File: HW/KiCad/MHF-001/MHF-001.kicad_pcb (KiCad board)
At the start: 2 copper layers, 100 x 100 mm, 204 parts, among them J1 DE15_Socket_HighDensity_Mount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, J11 PPTC081LFBN-RC, J12 M20-9980345, J2 Mini-DIN-6, J3 Conn_Coaxial, J4 PJ-102AH, J5 USB_C_Receptacle_USB2.0_16P, J6 M20-9980345, J7 M20-9980245, M3 CY7C109D-10ZXI, M5 CY7C109D-10ZXI, Q1 BC107, Q2 PMV48XP, U1 NCP1117-5.0_SOT223, U10 74HC245, U11 74HC245, U12 74HC245, U13 LMV358IDGKR, U14 LP2985-3.3, U15 ATMEGA16U2-MU, U2 74HC14, U3 74LS08, U4 74HC165, U5 ATmega2560-16A, U6 74AHC373PW, U7 74HC595, U8 74HC595, U9 74HC157, Y1 CSTNE16M0V530000R0, Y2 LFXTAL003240BULK

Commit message: +3d models, +Pins.rst, some reorganisation
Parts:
- removed C17: 22p, Capacitor_SMD:C_0603_1608Metric
- removed C18, C19: 100n, Capacitor_SMD:C_0603_1608Metric
- removed D4: CGRB307-G, Diode_SMD:D_SMB
- removed D5, D8: YELLOW, LED_SMD:LED_0805_2012Metric
- removed D6: GREEN, LED_SMD:LED_0805_2012Metric
- removed D7: CD1206-S01575, Diode_SMD:D_1206_3216Metric
- removed FB1, FB2: 1kΩ@100MHz, Inductor_SMD:L_0805_2012Metric
- removed FID1, FID2, FID3, FID4: Fiducial, Fiducial:Fiducial_1mm_Mask3mm
- removed J11: PPTC081LFBN-RC, Connector_PinSocket_2.54mm:PinSocket_1x08_P2.54mm_Vertical
- removed J12, J6: M20-9980345, Connector_PinHeader_2.54mm:PinHeader_2x03_P2.54mm_Vertical
- removed J4: PJ-102AH, Connector_BarrelJack:BarrelJack_Kycon_KLDX-0202-xC_Horizontal
- removed J7: M20-9980245, Arduino Mega 2560:CONN_M20-9980245_HRW
- removed Q2: PMV48XP, Package_TO_SOT_SMD:SC-59
- removed RN1, RN5: 10k, Resistor_SMD:R_Array_Convex_4x0612
- removed RN2: 22R, Resistor_SMD:R_Array_Convex_4x0612
- removed RN3, RN4: 1k, Resistor_SMD:R_Array_Convex_4x0612
- removed RV1, RV2: 5pF@1MHz, Resistor_SMD:R_0603_1608Metric
- removed U5: ATmega2560-16A, Package_QFP:TQFP-100_14x14mm_P0.5mm
- added H1: MountingHole, MountingHole:MountingHole_3.2mm_M3, F.Cu at (31.6, 29.6)
- added H2: MountingHole, MountingHole:MountingHole_3.2mm_M3, F.Cu at (118.9, 30.5)
- added H3: MountingHole, MountingHole:MountingHole_3.2mm_M3, F.Cu at (122.8, 106.6)
- added H4: MountingHole, MountingHole:MountingHole_3.2mm_M3, F.Cu at (38.7, 107.7)
- added J8: AVR-ISP-6, Connector_PinHeader_2.54mm:PinHeader_2x03_P2.54mm_Vertical, F.Cu at (160.4, 118.9)
- added LED1: LED, LED_SMD:LED_0201_0603Metric, F.Cu at (166.7, 117.5)
- added LED2: LED, LED_SMD:LED_0201_0603Metric, F.Cu at (166.7, 119.2)
- added LED3: LED, LED_SMD:LED_0201_0603Metric, F.Cu at (166.7, 121.0)
- added LED4: LED, LED_SMD:LED_0201_0603Metric, F.Cu at (166.7, 122.7)
- added R28: 1k, Resistor_SMD:R_0603_1608Metric, F.Cu at (151.0, 90.3)
- added R29: 1M, Resistor_SMD:R_0603_1608Metric, F.Cu at (151.0, 92.8)
- added R30: 22, Resistor_SMD:R_0603_1608Metric, F.Cu at (151.0, 95.3)
- added R31: 22, Resistor_SMD:R_0603_1608Metric, F.Cu at (151.0, 97.8)
- added R32: ---, Resistor_SMD:R_0603_1608Metric, F.Cu at (151.0, 100.3)
- added R33: ---, Resistor_SMD:R_0603_1608Metric, F.Cu at (151.0, 102.9)
- added R34: 6k8, Resistor_SMD:R_0603_1608Metric, F.Cu at (155.0, 85.3)
- added R35: 6k8, Resistor_SMD:R_0603_1608Metric, F.Cu at (155.0, 87.8)
- added R36: 1k, Resistor_SMD:R_0603_1608Metric, F.Cu at (155.0, 90.3)
- added R37: 10k, Resistor_SMD:R_0603_1608Metric, F.Cu at (155.0, 92.8)
- C11: value 100n -> 10M; footprint Capacitor_SMD:C_0603_1608Metric -> Capacitor_SMD:C_1206_3216Metric
- C12, C15: value 1u -> 100n
- C16: value 22p -> 100n
- C2, C7: value 47u -> 100n; footprint Arduino Mega 2560:CAP_EEHZA1E470P -> Capacitor_SMD:C_0603_1608Metric
- D2: value YELLOW -> D; footprint LED_SMD:LED_0805_2012Metric -> Diode_SMD:D_1206_3216Metric
- D3: value CD1206-S01575 -> D; footprint Diode_SMD:D_1206_3216Metric -> Diode_SMD:D_1210_3225Metric
- F1: value MF-MSMF050-2 -> Polyfuse; footprint Fuse:Fuse_1812_4532Metric_Pad1.30x3.40mm_HandSolder -> Fuse:Fuse_1206_3216Metric_Pad1.42x1.75mm_HandSolder
- J5: value USB_C_Receptacle_USB2.0_16P -> USB_B_Micro; footprint Connector_USB:USB_C_Receptacle_GCT_USB4105-xx-A_16P_TopMnt_Horizontal -> Connector_USB:USB_Micro-B_XKB_U254-051T-4BH83-F1S
- JP89, JP90: value SolderJumper_2_Open -> SolderJumper_2_Bridged; footprint Jumper:SolderJumper-2_P1.3mm_Open_Pad1.0x1.5mm -> Jumper:SolderJumper-2_P1.3mm_Bridged_Pad1.0x1.5mm
- R24: value 1M -> 22
- R25: value 5k1 -> 22
- R26: value 5k1 -> 10k
- U1: value NCP1117-5.0_SOT223 -> ATMEGA2560-16AU; footprint Package_TO_SOT_SMD:SOT-223-3_TabPin2 -> Package_QFP:TQFP-100_14x14mm_P0.5mm
- U13: value LMV358IDGKR -> CH340G; footprint Package_SO:MSOP-8_3x3mm_P0.65mm -> Package_SO:SOIC-16_3.9x9.9mm_P1.27mm
- U14: value LP2985-3.3 -> AMS1117-5.0; footprint Package_TO_SOT_SMD:SOT-23-5 -> Package_TO_SOT_SMD:SOT-223-3_TabPin2
- U15: value ATMEGA16U2-MU -> AMS1117-3.3; footprint Package_DFN_QFN:VQFN-32-1EP_5x5mm_P0.5mm_EP3.1x3.1mm -> Package_TO_SOT_SMD:SOT-223-3_TabPin2
- Y1: value CSTNE16M0V530000R0 -> 16 MHz; footprint Crystal:Resonator_SMD_Murata_CSTxExxV-3Pin_3.0x1.1mm -> Crystal:Crystal_SMD_HC49-SD
- Y2: value LFXTAL003240BULK -> 12 MHz; footprint Crystal:Crystal_HC49-4H_Vertical -> Crystal:Crystal_SMD_HC49-SD
- moved U1 185.2 mm to (65.3, 94.9)
- moved JP89 163.0 mm to (1.68, 1.27)
- moved JP90 163.0 mm to (1.68, 4.83)
- moved J5 161.1 mm to (30.0, 99.5), turned to -90 degrees
- moved S1 132.6 mm to (156.6, 130.4)
- moved F1 115.7 mm to (171.0, 135.7)
- moved U15 100.7 mm to (145.9, 116.6)
- moved C16 94.7 mm to (147.0, 97.8)
- moved U7 93.9 mm to (-12.2, 96.2), turned to 0 degrees
- moved D3 92.7 mm to (170.8, 118.8)
- moved R24 92.3 mm to (147.0, 100.3)
- moved R26 92.2 mm to (151.0, 85.3)
- moved R25 91.7 mm to (147.0, 102.9)
- moved R27 91.7 mm to (151.0, 87.8)
- moved C5 91.5 mm to (143.0, 92.8)
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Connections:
- net Net-(JP16-B) renamed VGA Latch
- net Net-(JP41-B) renamed VGA data 0
- net Net-(JP42-B) renamed VGA data 1
- net Net-(JP43-B) renamed VGA data 2
- net Net-(JP44-B) renamed VGA data 3
- net Net-(JP45-B) renamed VGA data 4
- net Net-(JP46-B) renamed VGA data 5
- net Net-(JP47-B) renamed VGA data 6
- net Net-(JP48-B) renamed VGA data 7
- C10 pad 1: USBVCC -> +5V
- C11 pad 1: +5V -> Net-(D3-K)
- C12 pad 1: Net-(U15-UCAP) -> Reset
- C13 pad 2: +5V -> XTAL1
- C14 pad 2: CMP -> XTAL2
- C15 pad 1: GND -> +5V
- C15 pad 2: +3.3V -> GND
- C16 pad 1: Net-(U15-XTAL1) -> +3.3V
- C2 pad 1: VCC -> GND
- C2 pad 2: GND -> Net-(U13-V3)
- C3 pad 1: RESET -> GND
- C3 pad 2: GND -> Net-(U13-XO)
- C4 pad 1: VCC -> GND
- C4 pad 2: GND -> Net-(U13-XI)
- C9 pad 1: +5V -> Reset
- C9 pad 2: GND -> Net-(U13-~{DTR})
- D2 pad 1: TXL -> +5V
- D2 pad 2: Net-(D2-A) -> Reset
- D3 pad 1: +5V -> Net-(D3-K)
- D3 pad 2: RESET2 -> VIN
- F1 pad 1: USBVCC -> +5V
- F1 pad 2: XVCC -> Net-(J5-VBUS)
- JP10 pad 2: unconnected-(JP10-B-Pad2) -> SCK
- JP11 pad 2: unconnected-(JP11-B-Pad2) -> MOSI
- JP12 pad 2: unconnected-(JP12-B-Pad2) -> MISO
- JP25 pad 2: unconnected-(JP25-B-Pad2) -> SCL
- JP26 pad 2: unconnected-(JP26-B-Pad2) -> SDA
- JP33 pad 2: unconnected-(JP33-B-Pad2) -> TX
- JP34 pad 2: unconnected-(JP34-B-Pad2) -> RX
- JP35 pad 2: unconnected-(JP35-B-Pad2) -> CTS
- JP36 pad 2: Inside -> RTS
- JP39 pad 2: unconnected-(JP39-B-Pad2) -> Inside
- JP49 pad 2: unconnected-(JP49-B-Pad2) -> WE
- JP50 pad 2: unconnected-(JP50-B-Pad2) -> RD
- JP51 pad 2: unconnected-(JP51-B-Pad2) -> ALE
- JP52 pad 2: unconnected-(JP52-B-Pad2) -> XAA16
- JP57 pad 2: unconnected-(JP57-B-Pad2) -> Ib
- JP58 pad 2: unconnected-(JP58-B-Pad2) -> Bb
- JP59 pad 2: unconnected-(JP59-B-Pad2) -> Gb
- JP60 pad 2: unconnected-(JP60-B-Pad2) -> Rb
- JP61 pad 2: unconnected-(JP61-B-Pad2) -> If
- JP62 pad 2: unconnected-(JP62-B-Pad2) -> Bf
- JP63 pad 2: unconnected-(JP63-B-Pad2) -> Gf
- JP64 pad 2: unconnected-(JP64-B-Pad2) -> Rf
- JP89 pad 1: GND -> PS2 Clock
- JP89 pad 2: GND -> Net-(D1-K)
- JP9 pad 2: unconnected-(JP9-B-Pad2) -> SS
- JP90 pad 1: RESET -> PS2 Data
- JP90 pad 2: RESET -> /Data
- M3 pad 10: PG3 -> XAA16
- M3 pad 32: PG0 -> RD
- M3 pad 5: PG1 -> WE
- M5 pad 10: unconnected-(M5-A16-Pad10) -> XAA16
- M5 pad 7: unconnected-(M5-A15-Pad7) -> Shared_Address_A15
- R16 pad 2: Mega_6309_data0 -> Ib
- R17 pad 2: Mega_6309_data1 -> Bb
- R18 pad 2: Mega_6309_data2 -> Gb
- R19 pad 2: Mega_6309_data3 -> Rb
- R20 pad 2: Mega_6309_data4 -> If
- R21 pad 2: Mega_6309_data5 -> Bf
- R22 pad 2: Mega_6309_data6 -> Gf
- R23 pad 2: Mega_6309_data7 -> Rf
- R24 pad 1: XTAL1 -> RD+
- R24 pad 2: XTAL2 -> Net-(J5-D+)
- R25 pad 1: GND -> RD-
- R25 pad 2: CC1 -> Net-(J5-D-)
- R26 pad 1: GND -> +5V
- R26 pad 2: CC2 -> Reset
- R27 pad 1: Net-(U15-XTAL1) -> Net-(U13-XI)
- R27 pad 2: Net-(U15-PC0) -> Net-(U13-XO)
- R5 pad 1: SIGNAL_RCA -> Bb
- S1 pad 3: RESET -> Reset
- S1 pad 4: RESET -> Reset
- S1 pad 5: unconnected-(S1-Pad5) -> GND
- U1 pad 1: GND -> PG5
- U1 pad 2: +5V -> PE0
- U1 pad 3: VCC -> PE1
- U13 pad 1: L13 -> GND
- U13 pad 2: L13 -> M8TXD
- U13 pad 3: PB7 -> M8RXD
- U13 pad 4: GND -> Net-(U13-V3)
- U13 pad 5: CMP -> RD+
- U13 pad 6: +3.3V -> RD-
- U13 pad 7: GATE_CMD -> Net-(U13-XI)
- U13 pad 8: +5V -> Net-(U13-XO)
- U14 pad 1: +5V -> GND
- U14 pad 2: GND -> +5V
- U14 pad 3: +5V -> Net-(D3-K)
- U15 pad 1: Net-(U15-XTAL1) -> GND
- U15 pad 2: Net-(U15-PC0) -> +3.3V
- U15 pad 3: GND -> +5V
- U3 pad 1: SIGNAL_RCA -> Bb
- U6 pad 11: PG2 -> ALE
- U9 pad 10: unconnected-(U9-I1c-Pad10) -> Gf
- U9 pad 11: unconnected-(U9-I0c-Pad11) -> Gb
- U9 pad 13: unconnected-(U9-I1d-Pad13) -> Bf
- U9 pad 14: unconnected-(U9-I0d-Pad14) -> Bb
- U9 pad 2: unconnected-(U9-I0a-Pad2) -> Ib
- U9 pad 3: unconnected-(U9-I1a-Pad3) -> If
- U9 pad 5: unconnected-(U9-I0b-Pad5) -> Rb
- U9 pad 6: unconnected-(U9-I1b-Pad6) -> Rf
- Y1 pad 2: GND -> XTAL1
- Y2 pad 1: Net-(U15-PC0) -> Net-(U13-XO)
- Y2 pad 2: Net-(U15-XTAL1) -> Net-(U13-XI)

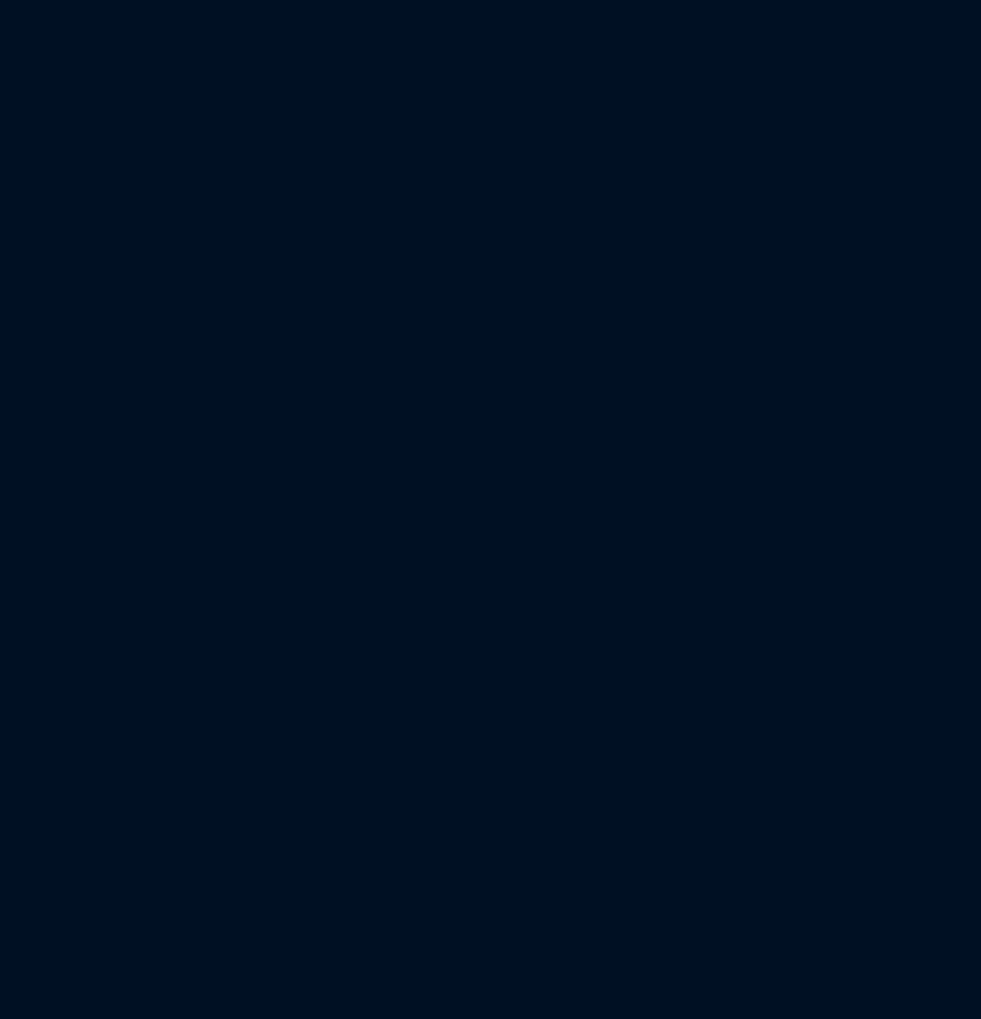
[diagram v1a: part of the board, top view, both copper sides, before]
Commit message: +Comp24 footprint
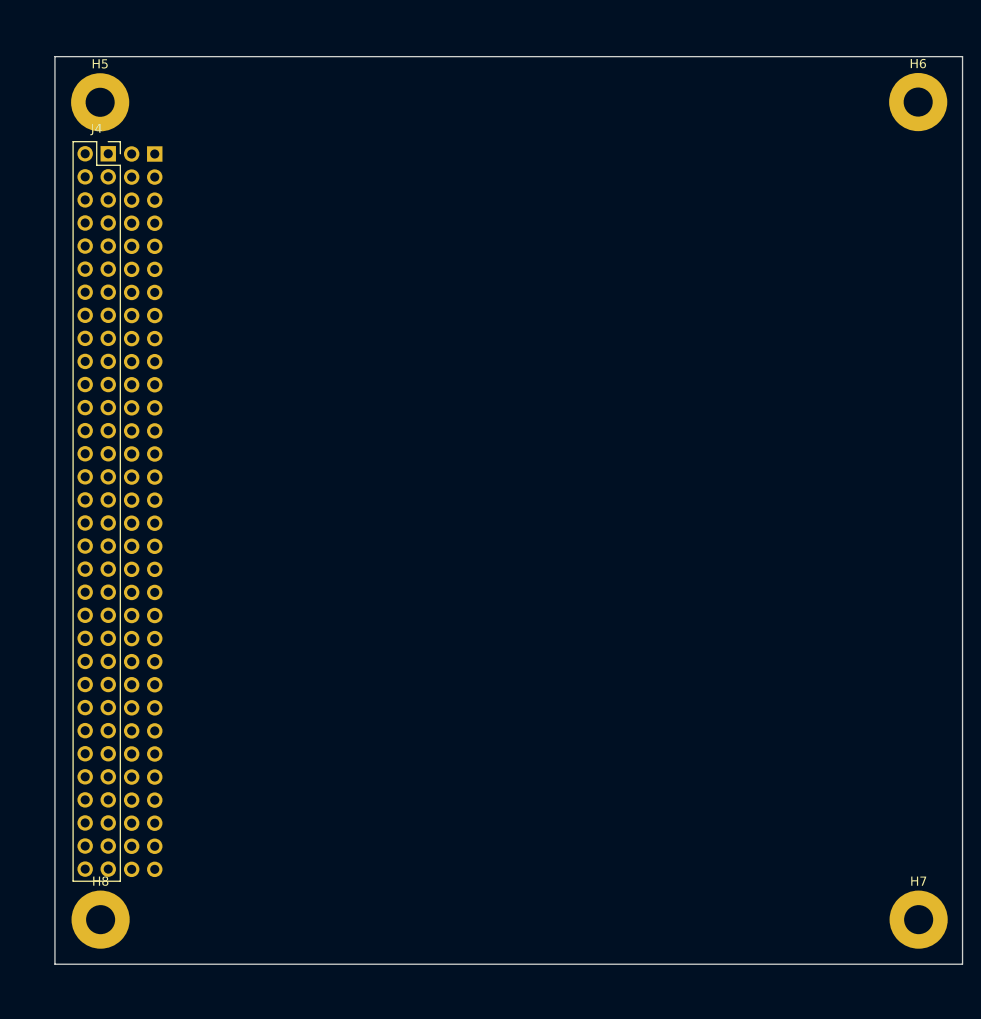
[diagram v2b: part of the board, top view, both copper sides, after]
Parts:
- added H5: MountingHole, MountingHole:MountingHole_3.2mm_M3_Pad, F.Cu at (186.1, 24.5)
- added H6: MountingHole, MountingHole:MountingHole_3.2mm_M3_Pad, F.Cu at (276.2, 24.5)
- added H7: MountingHole, MountingHole:MountingHole_3.2mm_M3_Pad, F.Cu at (276.2, 114.5)
- added H8: MountingHole, MountingHole:MountingHole_3.2mm_M3_Pad, F.Cu at (186.2, 114.5)
- added J4: Conn_02x32_Odd_Even, Connector_PinSocket_2.54mm:PinSocket_2x32_P2.54mm_Vertical, F.Cu at (187.0, 30.2)
- added J6: Conn_02x32_Odd_Even, Connector_PinHeader_2.54mm:PinHeader_2x32_P2.54mm_Vertical, B.Cu at (192.1, 30.2)
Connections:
- net /Data renamed Data
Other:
- board size 100 x 100 mm -> 252.9 x 100.2 mm

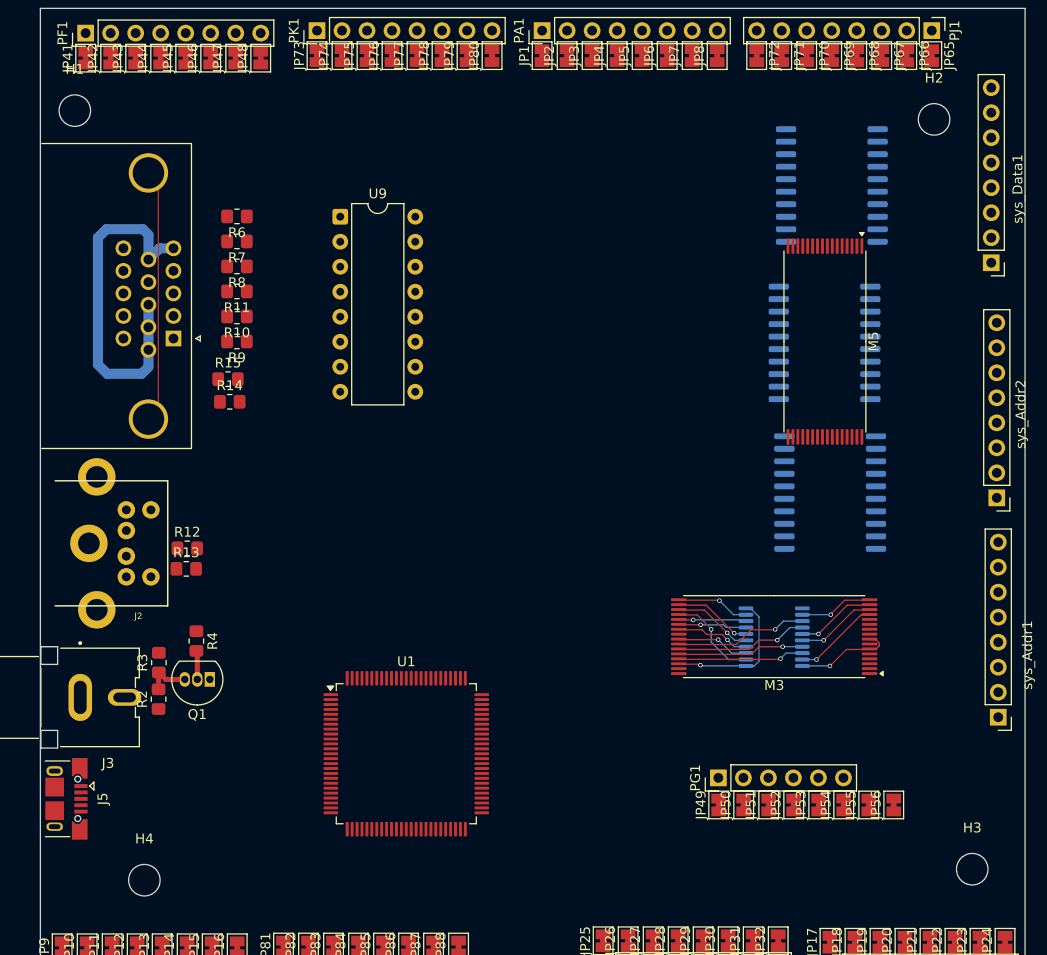
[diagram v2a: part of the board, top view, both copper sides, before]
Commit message: - mounting holes
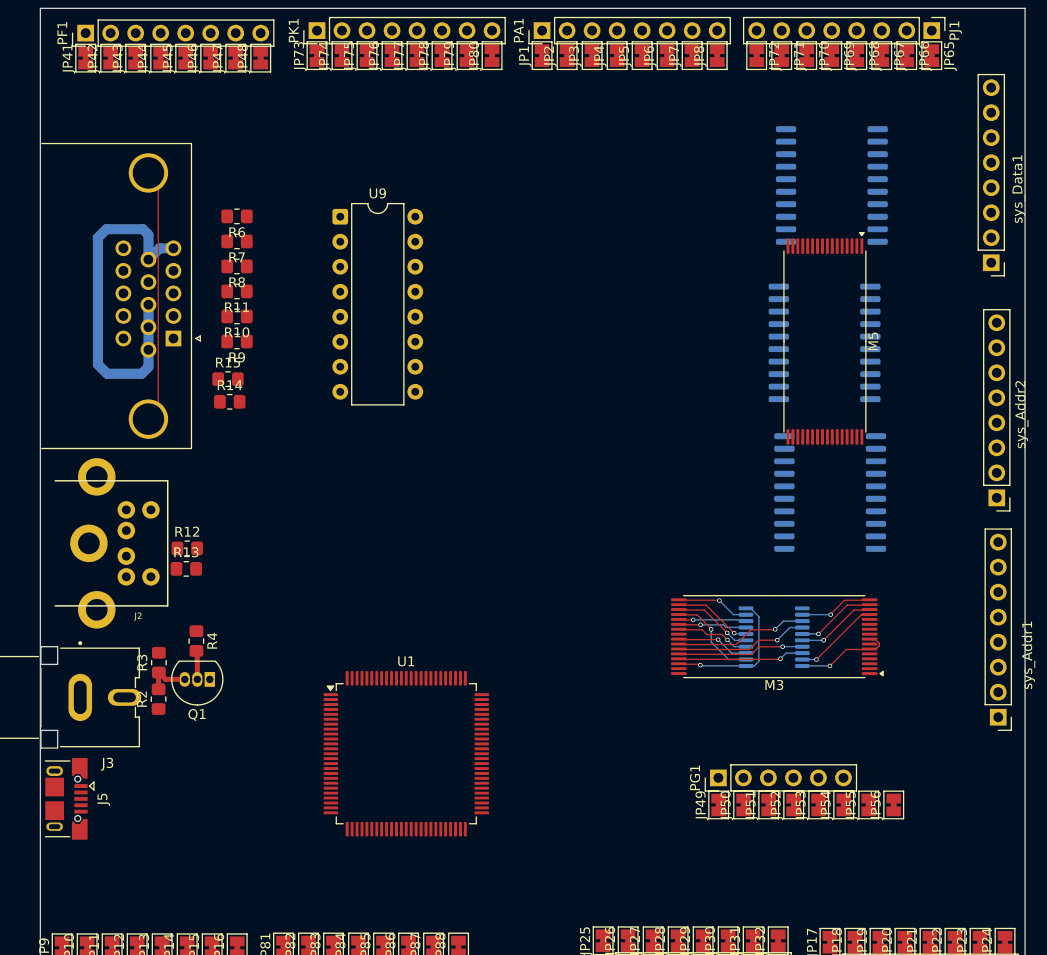
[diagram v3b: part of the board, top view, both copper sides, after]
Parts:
- removed H1, H2, H3, H4: MountingHole, MountingHole:MountingHole_3.2mm_M3

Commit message: schema MHF-001 maybe OK
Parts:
- removed sys_Addr1, sys_Addr2, sys_Data1: Conn_01x08, Connector_PinHeader_2.54mm:PinHeader_1x08_P2.54mm_Vertical
- added J10: I2C, Connector_PinHeader_2.54mm:PinHeader_1x04_P2.54mm_Vertical, F.Cu at (139.7, 142.2)
- added J11: POWER, Connector_PinHeader_2.54mm:PinHeader_2x03_P2.54mm_Vertical, F.Cu at (132.1, 160.0)
- added J7: SPI, Connector_PinHeader_2.54mm:PinHeader_1x06_P2.54mm_Vertical, F.Cu at (132.1, 142.2)
- added J9: Serial, Connector_PinHeader_2.54mm:PinHeader_1x06_P2.54mm_Vertical, F.Cu at (134.6, 142.2)
- added JP100: SolderJumper_3_Open, Jumper:SolderJumper-3_P1.3mm_Open_RoundedPad1.0x1.5mm, F.Cu at (127.0, 152.4)
- added JP101: SolderJumper_3_Open, Jumper:SolderJumper-3_P1.3mm_Open_RoundedPad1.0x1.5mm, F.Cu at (127.0, 157.5)
- added JP102: SolderJumper_3_Open, Jumper:SolderJumper-3_P1.3mm_Open_RoundedPad1.0x1.5mm, F.Cu at (95.5, 141.5)
- added JP103: SolderJumper_3_Open, Jumper:SolderJumper-3_P1.3mm_Open_RoundedPad1.0x1.5mm, F.Cu at (95.5, 146.6)
- added JP104: SolderJumper_3_Open, Jumper:SolderJumper-3_P1.3mm_Open_RoundedPad1.0x1.5mm, F.Cu at (95.5, 149.1)
- added JP105: SolderJumper_3_Open, Jumper:SolderJumper-3_P1.3mm_Open_RoundedPad1.0x1.5mm, F.Cu at (95.5, 154.2)
- added JP106: SolderJumper_3_Open, Jumper:SolderJumper-3_P1.3mm_Open_RoundedPad1.0x1.5mm, F.Cu at (95.5, 156.7)
- added JP107: SolderJumper_3_Open, Jumper:SolderJumper-3_P1.3mm_Open_RoundedPad1.0x1.5mm, F.Cu at (95.5, 161.8)
- added JP108: SolderJumper_3_Open, Jumper:SolderJumper-3_P1.3mm_Open_RoundedPad1.0x1.5mm, F.Cu at (95.5, 164.4)
- added JP92: SolderJumper_3_Open, Jumper:SolderJumper-3_P1.3mm_Open_RoundedPad1.0x1.5mm, F.Cu at (119.4, 142.2)
- added JP93: SolderJumper_3_Open, Jumper:SolderJumper-3_P1.3mm_Open_RoundedPad1.0x1.5mm, F.Cu at (119.4, 144.8)
- added JP94: SolderJumper_3_Open, Jumper:SolderJumper-3_P1.3mm_Open_RoundedPad1.0x1.5mm, F.Cu at (119.4, 149.9)
- added JP95: SolderJumper_3_Open, Jumper:SolderJumper-3_P1.3mm_Open_RoundedPad1.0x1.5mm, F.Cu at (119.4, 152.4)
- added JP96: SolderJumper_3_Open, Jumper:SolderJumper-3_P1.3mm_Open_RoundedPad1.0x1.5mm, F.Cu at (119.4, 157.5)
- added JP97: SolderJumper_3_Open, Jumper:SolderJumper-3_P1.3mm_Open_RoundedPad1.0x1.5mm, F.Cu at (127.0, 142.2)
- added JP98: SolderJumper_3_Open, Jumper:SolderJumper-3_P1.3mm_Open_RoundedPad1.0x1.5mm, F.Cu at (127.0, 144.8)
- added JP99: SolderJumper_3_Open, Jumper:SolderJumper-3_P1.3mm_Open_RoundedPad1.0x1.5mm, F.Cu at (127.0, 149.9)
- added LED5: LED, LED_SMD:LED_0805_2012Metric, F.Cu at (100.5, 146.6)
- added LED6: LED, LED_SMD:LED_0805_2012Metric, F.Cu at (105.0, 146.7)
- added R38: 1k, Resistor_SMD:R_0805_2012Metric_Pad1.20x1.40mm_HandSolder, F.Cu at (100.5, 141.5)
- added R39: 1k, Resistor_SMD:R_0805_2012Metric_Pad1.20x1.40mm_HandSolder, F.Cu at (100.5, 144.0)
- C10, C12, C13, C14, C15, C16, C2, C3, C4, C5, C6, C7, C8, C9: footprint Capacitor_SMD:C_0603_1608Metric -> Capacitor_SMD:C_0603_1608Metric_Pad1.08x0.95mm_HandSolder
- C11: footprint Capacitor_SMD:C_1206_3216Metric -> Capacitor_SMD:C_0603_1608Metric_Pad1.08x0.95mm_HandSolder
- J6: value Conn_02x32_Odd_Even -> 02x32
- LED1, LED2, LED3, LED4: footprint LED_SMD:LED_0201_0603Metric -> LED_SMD:LED_0805_2012Metric
- R24, R25, R26, R27, R28, R29, R30, R31, R32, R33, R34, R35, R36, R37: footprint Resistor_SMD:R_0603_1608Metric -> Resistor_SMD:R_0603_1608Metric_Pad0.98x0.95mm_HandSolder
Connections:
- net Data renamed /Data
- net Net-(U11-A->B) renamed G_A_DIR
- J4 pad 1: D0 -> +5V
- J4 pad 10: unconnected-(J4-Pin_10-Pad10) -> D7
- J4 pad 11: unconnected-(J4-Pin_11-Pad11) -> A0
- J4 pad 12: unconnected-(J4-Pin_12-Pad12) -> A1
- J4 pad 13: unconnected-(J4-Pin_13-Pad13) -> A2
- J4 pad 14: unconnected-(J4-Pin_14-Pad14) -> A3
- J4 pad 15: unconnected-(J4-Pin_15-Pad15) -> A4
- J4 pad 16: unconnected-(J4-Pin_16-Pad16) -> A5
- J4 pad 17: unconnected-(J4-Pin_17-Pad17) -> A6
- J4 pad 18: unconnected-(J4-Pin_18-Pad18) -> A7
- J4 pad 19: unconnected-(J4-Pin_19-Pad19) -> A8
- J4 pad 2: D1 -> +5V
- J4 pad 20: unconnected-(J4-Pin_20-Pad20) -> A9
- J4 pad 21: unconnected-(J4-Pin_21-Pad21) -> A10
- J4 pad 22: unconnected-(J4-Pin_22-Pad22) -> A11
- J4 pad 23: unconnected-(J4-Pin_23-Pad23) -> A12
- J4 pad 24: unconnected-(J4-Pin_24-Pad24) -> A13
- J4 pad 25: unconnected-(J4-Pin_25-Pad25) -> A14
- J4 pad 26: unconnected-(J4-Pin_26-Pad26) -> A15
- J4 pad 27: unconnected-(J4-Pin_27-Pad27) -> A16
- J4 pad 28: unconnected-(J4-Pin_28-Pad28) -> B16
- J4 pad 29: unconnected-(J4-Pin_29-Pad29) -> A_BUS
- J4 pad 3: D2 -> D0
- J4 pad 30: unconnected-(J4-Pin_30-Pad30) -> B_BUS
- J4 pad 31: unconnected-(J4-Pin_31-Pad31) -> A_HALT
- J4 pad 32: unconnected-(J4-Pin_32-Pad32) -> B_HALT
- J4 pad 33: unconnected-(J4-Pin_33-Pad33) -> A_READ
- J4 pad 34: unconnected-(J4-Pin_34-Pad34) -> B_READ
- J4 pad 35: unconnected-(J4-Pin_35-Pad35) -> A_WRITE
- J4 pad 36: unconnected-(J4-Pin_36-Pad36) -> B_WRITE
- J4 pad 37: unconnected-(J4-Pin_37-Pad37) -> A_SHARE_BUSY
- J4 pad 38: unconnected-(J4-Pin_38-Pad38) -> B_SHARE_BUSY
- J4 pad 39: unconnected-(J4-Pin_39-Pad39) -> A_SHARE_DIRTY
- J4 pad 4: D3 -> D1
- J4 pad 40: unconnected-(J4-Pin_40-Pad40) -> B_SHARE_DIRTY
- J4 pad 41: unconnected-(J4-Pin_41-Pad41) -> A_SHARE_GRANTED
- J4 pad 42: unconnected-(J4-Pin_42-Pad42) -> B_SHARE_GRANTED
- J4 pad 43: unconnected-(J4-Pin_43-Pad43) -> A_SHARE_REQUEST
- J4 pad 44: unconnected-(J4-Pin_44-Pad44) -> B_SHARE_REQUEST
- J4 pad 45: unconnected-(J4-Pin_45-Pad45) -> A_SHARE_WANTED
- J4 pad 46: unconnected-(J4-Pin_46-Pad46) -> B_SHARE_WANTED
- J4 pad 47: unconnected-(J4-Pin_47-Pad47) -> A_S_ENABLE
- J4 pad 48: unconnected-(J4-Pin_48-Pad48) -> B_S_ENABLE
- J4 pad 49: unconnected-(J4-Pin_49-Pad49) -> A_S_READ
- J4 pad 5: D4 -> D2
- J4 pad 50: unconnected-(J4-Pin_50-Pad50) -> B_S_READ
- J4 pad 51: unconnected-(J4-Pin_51-Pad51) -> A_S_WRITE
- J4 pad 52: unconnected-(J4-Pin_52-Pad52) -> B_S_WRITE
- J4 pad 53: unconnected-(J4-Pin_53-Pad53) -> A_G_D_DIR
- J4 pad 54: unconnected-(J4-Pin_54-Pad54) -> B_G_D_DIR
- J4 pad 55: unconnected-(J4-Pin_55-Pad55) -> A_G_D_OE
- J4 pad 56: unconnected-(J4-Pin_56-Pad56) -> B_G_D_OE
- J4 pad 57: unconnected-(J4-Pin_57-Pad57) -> A_G_A_DIR
- J4 pad 58: unconnected-(J4-Pin_58-Pad58) -> B_G_A_DIR
- J4 pad 59: unconnected-(J4-Pin_59-Pad59) -> A_G_A_OE
- J4 pad 6: unconnected-(J4-Pin_6-Pad6) -> D3
- J4 pad 60: unconnected-(J4-Pin_60-Pad60) -> B_G_A_OE
- J4 pad 63: unconnected-(J4-Pin_63-Pad63) -> GND
- J4 pad 64: unconnected-(J4-Pin_64-Pad64) -> GND
- J4 pad 7: D6 -> D4
- J4 pad 8: unconnected-(J4-Pin_8-Pad8) -> D5
- J4 pad 9: unconnected-(J4-Pin_9-Pad9) -> D6
- J5 pad 6: unconnected-(J5-Shield-Pad6) -> GND
- J6 pad 1: D0 -> +5V
- J6 pad 10: unconnected-(J6-Pin_10-Pad10) -> D7
- J6 pad 11: unconnected-(J6-Pin_11-Pad11) -> A0
- J6 pad 12: unconnected-(J6-Pin_12-Pad12) -> A1
- J6 pad 13: unconnected-(J6-Pin_13-Pad13) -> A2
- J6 pad 14: unconnected-(J6-Pin_14-Pad14) -> A3
- J6 pad 15: unconnected-(J6-Pin_15-Pad15) -> A4
- J6 pad 16: unconnected-(J6-Pin_16-Pad16) -> A5
- J6 pad 17: unconnected-(J6-Pin_17-Pad17) -> A6
- J6 pad 18: unconnected-(J6-Pin_18-Pad18) -> A7
- J6 pad 19: unconnected-(J6-Pin_19-Pad19) -> A8
- J6 pad 2: D1 -> +5V
- J6 pad 20: unconnected-(J6-Pin_20-Pad20) -> A9
- J6 pad 21: unconnected-(J6-Pin_21-Pad21) -> A10
- J6 pad 22: unconnected-(J6-Pin_22-Pad22) -> A11
- J6 pad 23: unconnected-(J6-Pin_23-Pad23) -> A12
- J6 pad 24: unconnected-(J6-Pin_24-Pad24) -> A13
- J6 pad 25: unconnected-(J6-Pin_25-Pad25) -> A14
- J6 pad 26: unconnected-(J6-Pin_26-Pad26) -> A15
- J6 pad 27: unconnected-(J6-Pin_27-Pad27) -> A16
- J6 pad 28: unconnected-(J6-Pin_28-Pad28) -> B16
- J6 pad 29: unconnected-(J6-Pin_29-Pad29) -> A_BUS
- J6 pad 3: D2 -> D0
- J6 pad 30: unconnected-(J6-Pin_30-Pad30) -> B_BUS
- J6 pad 31: unconnected-(J6-Pin_31-Pad31) -> A_HALT
- J6 pad 32: unconnected-(J6-Pin_32-Pad32) -> B_HALT
- J6 pad 33: unconnected-(J6-Pin_33-Pad33) -> A_READ
- J6 pad 34: unconnected-(J6-Pin_34-Pad34) -> B_READ
- J6 pad 35: unconnected-(J6-Pin_35-Pad35) -> A_WRITE
- J6 pad 36: unconnected-(J6-Pin_36-Pad36) -> B_WRITE
- J6 pad 37: unconnected-(J6-Pin_37-Pad37) -> A_SHARE_BUSY
- J6 pad 38: unconnected-(J6-Pin_38-Pad38) -> B_SHARE_BUSY
- J6 pad 39: unconnected-(J6-Pin_39-Pad39) -> A_SHARE_DIRTY
- J6 pad 4: D3 -> D1
- J6 pad 40: unconnected-(J6-Pin_40-Pad40) -> B_SHARE_DIRTY
- J6 pad 41: unconnected-(J6-Pin_41-Pad41) -> A_SHARE_GRANTED
- J6 pad 42: unconnected-(J6-Pin_42-Pad42) -> B_SHARE_GRANTED
- J6 pad 43: unconnected-(J6-Pin_43-Pad43) -> A_SHARE_REQUEST
- J6 pad 44: unconnected-(J6-Pin_44-Pad44) -> B_SHARE_REQUEST
- J6 pad 45: unconnected-(J6-Pin_45-Pad45) -> A_SHARE_WANTED
- J6 pad 46: unconnected-(J6-Pin_46-Pad46) -> B_SHARE_WANTED
- J6 pad 47: unconnected-(J6-Pin_47-Pad47) -> A_S_ENABLE
- J6 pad 48: unconnected-(J6-Pin_48-Pad48) -> B_S_ENABLE
- J6 pad 49: unconnected-(J6-Pin_49-Pad49) -> A_S_READ
- J6 pad 5: D4 -> D2
- J6 pad 50: unconnected-(J6-Pin_50-Pad50) -> B_S_READ
- J6 pad 51: unconnected-(J6-Pin_51-Pad51) -> A_S_WRITE
- J6 pad 52: unconnected-(J6-Pin_52-Pad52) -> B_S_WRITE
- J6 pad 53: unconnected-(J6-Pin_53-Pad53) -> A_G_D_DIR
- J6 pad 54: unconnected-(J6-Pin_54-Pad54) -> B_G_D_DIR
- J6 pad 55: unconnected-(J6-Pin_55-Pad55) -> A_G_D_OE
- J6 pad 56: unconnected-(J6-Pin_56-Pad56) -> B_G_D_OE
- J6 pad 57: unconnected-(J6-Pin_57-Pad57) -> A_G_A_DIR
- J6 pad 58: unconnected-(J6-Pin_58-Pad58) -> B_G_A_DIR
- J6 pad 59: unconnected-(J6-Pin_59-Pad59) -> A_G_A_OE
- J6 pad 6: unconnected-(J6-Pin_6-Pad6) -> D3
- J6 pad 60: unconnected-(J6-Pin_60-Pad60) -> B_G_A_OE
- J6 pad 63: unconnected-(J6-Pin_63-Pad63) -> GND
- J6 pad 64: unconnected-(J6-Pin_64-Pad64) -> GND
- J6 pad 7: D6 -> D4
- J6 pad 8: unconnected-(J6-Pin_8-Pad8) -> D5
- J6 pad 9: unconnected-(J6-Pin_9-Pad9) -> D6
- JP13 pad 2: unconnected-(JP13-B-Pad2) -> PS2-OE
- JP14 pad 2: unconnected-(JP14-B-Pad2) -> Shared_Address_A16
- JP27 pad 2: unconnected-(JP27-B-Pad2) -> /X_READ
- JP28 pad 2: unconnected-(JP28-B-Pad2) -> /X_WRITE
- JP29 pad 2: unconnected-(JP29-B-Pad2) -> /X_SHARE_BUSY
- JP30 pad 2: unconnected-(JP30-B-Pad2) -> /X_SHARE_DIRTY
- JP31 pad 2: unconnected-(JP31-B-Pad2) -> /X_SHARE_GRANTED
- JP32 pad 2: unconnected-(JP32-B-Pad2) -> /X_SHARE_REQUEST
- JP38 pad 2: unconnected-(JP38-B-Pad2) -> /X_SHARE_WANTED
- JP41 pad 2: VGA data 0 -> Mega_6309_data0
- JP42 pad 2: VGA data 1 -> Mega_6309_data1
- JP43 pad 2: VGA data 2 -> Mega_6309_data2
- JP44 pad 2: VGA data 3 -> Mega_6309_data3
- JP45 pad 2: VGA data 4 -> Mega_6309_data4
- JP46 pad 2: VGA data 5 -> Mega_6309_data5
- JP47 pad 2: VGA data 6 -> Mega_6309_data6
- JP48 pad 2: VGA data 7 -> Mega_6309_data7
- JP53 pad 2: unconnected-(JP53-B-Pad2) -> /X_HALT
- JP54 pad 2: unconnected-(JP54-B-Pad2) -> /X_BUS
- JP55 pad 1: unconnected-(JP55-A-Pad1) -> SCK
- JP55 pad 2: unconnected-(JP55-B-Pad2) -> PS2 Data
- JP56 pad 1: unconnected-(JP56-A-Pad1) -> MOSI
- JP56 pad 2: unconnected-(JP56-B-Pad2) -> PS2 Clock
- JP81 pad 2: Mega_6309_data0 -> VGA data 0
- JP82 pad 2: Mega_6309_data1 -> VGA data 1
- JP83 pad 2: Mega_6309_data2 -> VGA data 2
- JP84 pad 2: Mega_6309_data3 -> VGA data 3
- JP85 pad 2: Mega_6309_data4 -> SYNC_RCA
- JP86 pad 2: Mega_6309_data5 -> VGA data 5
- JP87 pad 2: Mega_6309_data6 -> VGA data 6
- JP88 pad 2: Mega_6309_data7 -> VGA data 7
- M5 pad 10: XAA16 -> Shared_Address_A16
- M5 pad 30: /~{MidRAM} -> GND
- M5 pad 32: /~{Read} -> S_READ
- M5 pad 5: /~{Write} -> S_WRITE
- M5 pad 6: unconnected-(M5-CS2/CE2-Pad6) -> S_ENABLE
- U10 pad 1: unconnected-(U10-A->B-Pad1) -> G_D_DIR
- U10 pad 19: Net-(U10-CE) -> G_D_OE
- U11 pad 19: Net-(U10-CE) -> G_A_OE
- U12 pad 19: Net-(U10-CE) -> G_A_OE
- U3 pad 2: ~{SUPRESS} -> VGA data 3
- U4 pad 3: VGA data 4 -> SYNC_RCA
- U7 pad 13: Net-(U7-~{OE}) -> PS2-OE
- U8 pad 13: Net-(U7-~{OE}) -> PS2-OE
